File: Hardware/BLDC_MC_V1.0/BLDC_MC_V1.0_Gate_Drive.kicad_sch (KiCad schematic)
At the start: 1 part, among them U6 DRV8353HRTAR

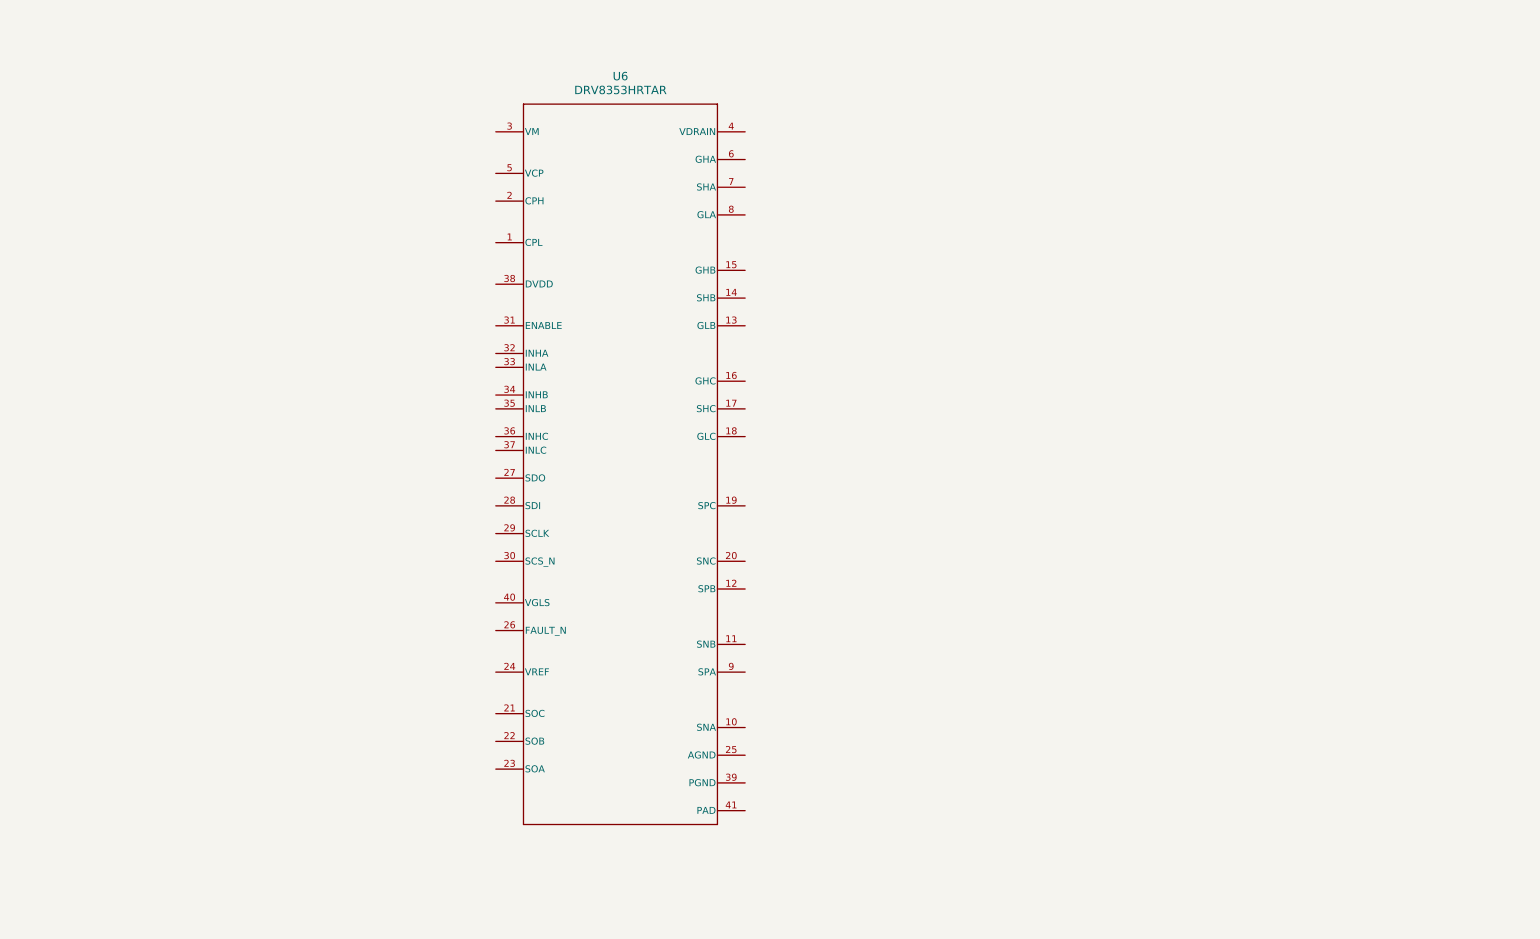
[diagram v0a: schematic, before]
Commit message: Edit the connection between sheets and add some details and connections to gatedrive sheet
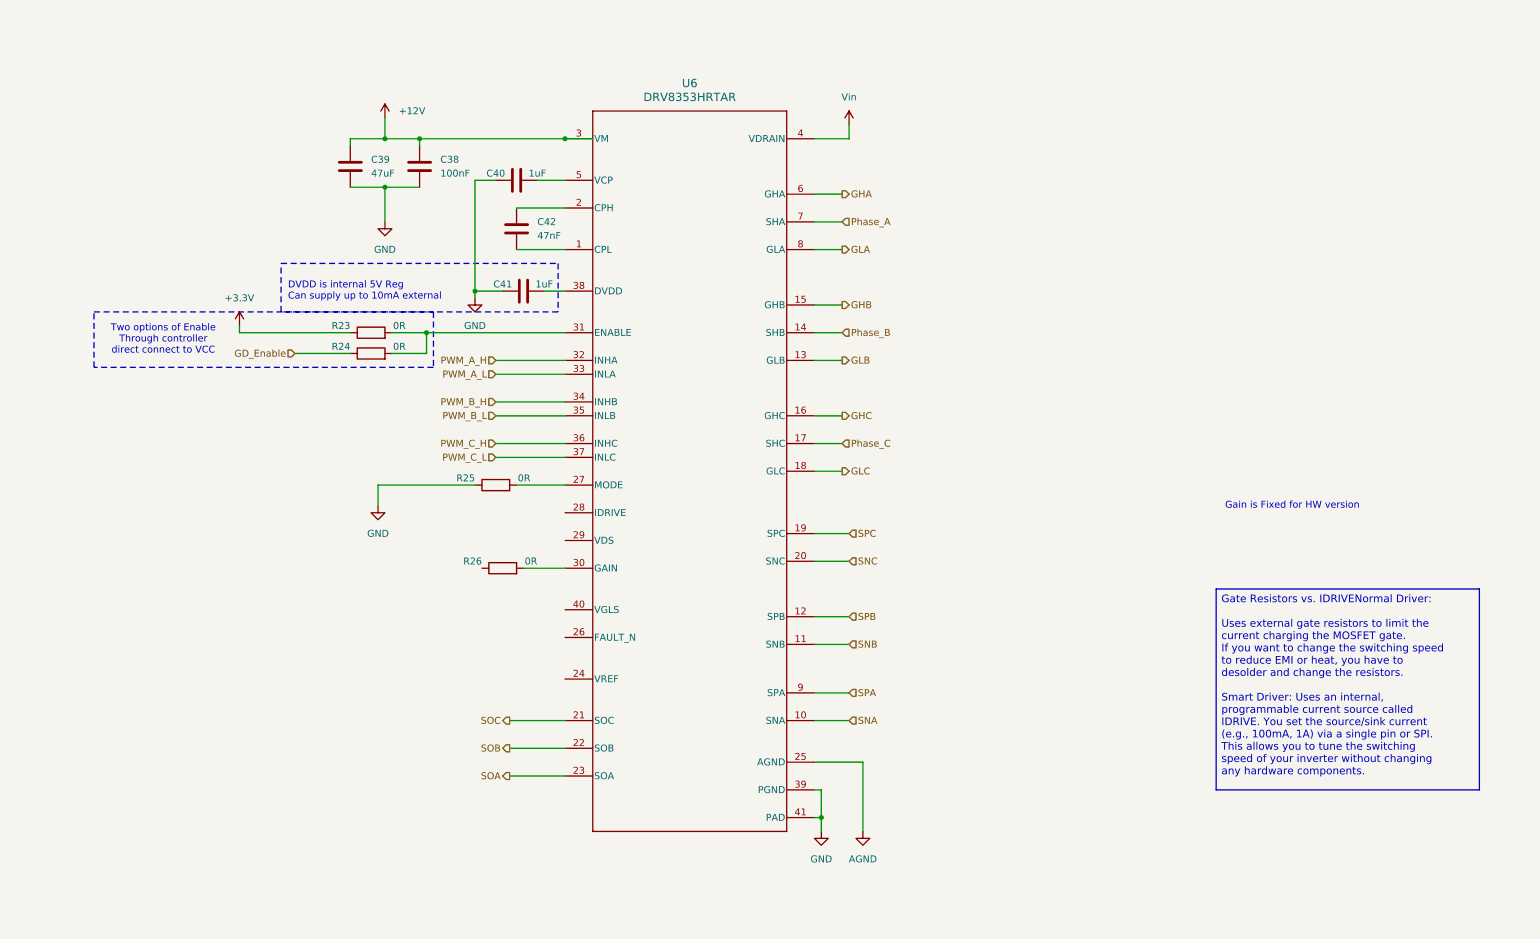
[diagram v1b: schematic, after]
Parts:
- added C38: 100nF, Capacitor_SMD:C_0805_2012Metric, symbol Device:C
- added C39: 47uF, Capacitor_SMD:C_1206_3216Metric, symbol Device:C
- added C40, C41: 1uF, Capacitor_SMD:C_0603_1608Metric, symbol Device:C
- added C42: 47nF, Capacitor_SMD:C_0603_1608Metric, symbol Device:C
- added R23, R24, R25, R26: 0R, Resistor_SMD:R_0603_1608Metric, symbol Device:R
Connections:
- net at U6.1 (CPL): now also C42.2
- net SNA: now reaches U6.10 (SNA)
- net SNB: now reaches U6.11 (SNB)
- net SPB: now reaches U6.12 (SPB)
- net GLB: now reaches U6.13 (GLB)
- net Phase_B: now reaches U6.14 (SHB)
- net GHB: now reaches U6.15 (GHB)
- net GHC: now reaches U6.16 (GHC)
- net Phase_C: now reaches U6.17 (SHC)
- net GLC: now reaches U6.18 (GLC)
- net SPC: now reaches U6.19 (SPC)
- net at U6.2 (CPH): now also C42.1
- net SNC: now reaches U6.20 (SNC)
- net SOC: now reaches U6.21 (SOC)
- net SOB: now reaches U6.22 (SOB)
- net SOA: now reaches U6.23 (SOA)
- net AGND: now reaches U6.25 (AGND)
- net at U6.27 (MODE): now also R25.2
- net +12V: now reaches U6.3 (VM)
- net +12V: now also C38.1, C39.2
- net at U6.30 (GAIN): now also R26.2
- net at U6.31 (ENABLE): now also R23.2, R24.2
- net PWM_A_H: now reaches U6.32 (INHA)
- net PWM_A_L: now reaches U6.33 (INLA)
- net PWM_B_H: now reaches U6.34 (INHB)
- net PWM_B_L: now reaches U6.35 (INLB)
- net PWM_C_H: now reaches U6.36 (INHC)
- net PWM_C_L: now reaches U6.37 (INLC)
- net at U6.38 (DVDD): now also C41.2
- net GND: now reaches U6.39 (PGND)
- net GND: now also U6.41 (PAD), C38.2, C39.1, C40.1, C41.1, R25.1
- net Vin: now reaches U6.4 (VDRAIN)
- net at U6.5 (VCP): now also C40.2
- net GHA: now reaches U6.6 (GHA)
- net Phase_A: now reaches U6.7 (SHA)
- net GLA: now reaches U6.8 (GLA)
- net SPA: now reaches U6.9 (SPA)
- new net +3.3V: R23.1
- new net GD_Enable: R24.1
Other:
- note added: "DVDD is internal 5V Reg Can supply up to 10mA external"
- note added: "Gain is Fixed for HW version"
- note added: "Two options of Enable Through controller direct connect to VCC"
- moved on the sheet: U6

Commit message: Restore the importenat project files from last commit and define the routing of current sensor as differntial pair
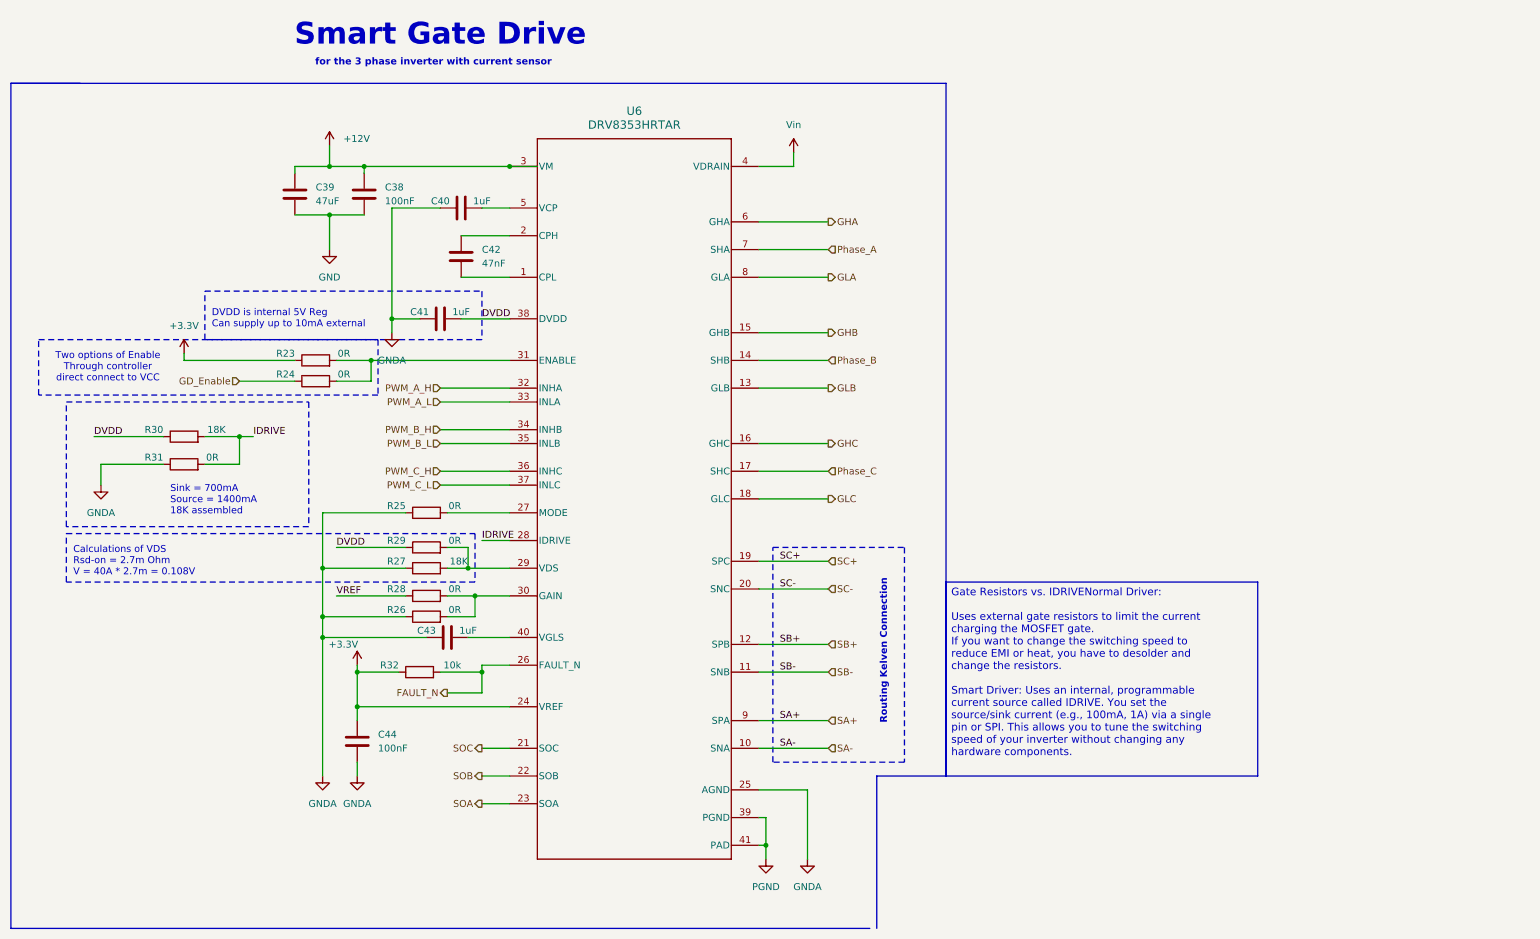
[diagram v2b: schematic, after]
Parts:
- added C43: 1uF, Capacitor_SMD:C_0603_1608Metric, symbol Device:C
- added C44: 100nF, Capacitor_SMD:C_0805_2012Metric, symbol Device:C
- added R27, R30: 18K, Resistor_SMD:R_0603_1608Metric, symbol Device:R
- added R28, R29, R31: 0R, Resistor_SMD:R_0603_1608Metric, symbol Device:R
- added R32: 10k, Resistor_SMD:R_0603_1608Metric, symbol Device:R
- R25: Assembled No -> Yes
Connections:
- net AGND is gone; now on net GNDA: U6.25 (AGND)
- net +3.3V: now also U6.24 (VREF), C44.1, R32.1
- net GND: no longer C40.1, C41.1, R25.1, U6.39 (PGND), U6.41 (PAD)
- net DVDD: now reaches C41.2, U6.38 (DVDD)
- net DVDD: now also R29.1, R30.1
- net FAULT_N: now reaches U6.26 (FAULT_N)
- net FAULT_N: now also R32.2
- net IDRIVE: now reaches U6.28 (IDRIVE)
- net IDRIVE: now also R30.2, R31.2
- net at U6.29 (VDS): now also R27.2, R29.2
- net at R26.2, U6.30 (GAIN): now also R28.2
- net at U6.40 (VGLS): now also C43.2
- net GNDA: now reaches R26.1
- net GNDA: now also C40.1, C41.1, R25.1, C43.1, C44.2, R27.1, R31.1
- net SNA renamed SA-
- net SNB renamed SB-
- net SNC renamed SC-
- net SPA renamed SA+
- net SPB renamed SB+
- net SPC renamed SC+
- new net PGND: U6.39 (PGND), U6.41 (PAD)
- new net VREF: R28.1
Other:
- note added: "Calculations of VDS Rsd-on = 2.7m Ohm V = 40A * 2.7m = 0.108V"
- note added: "Routing Kelven Connection"
- note added: "Sink = 700mA Source = 1400mA 18K assembled"
- note added: "Smart Gate Drive"
- note added: "for the 3 phase inverter with current sensor"
- note removed: "Gain is Fixed for HW version"
- moved on the sheet: C38, C39, C40, C41, C42, R23, R24, R25, R26, U6

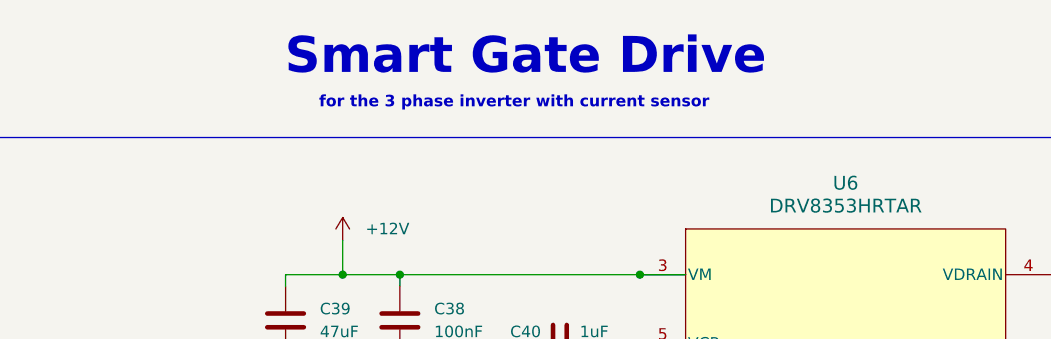
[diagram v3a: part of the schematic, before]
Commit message: Adjust the connections between sheets
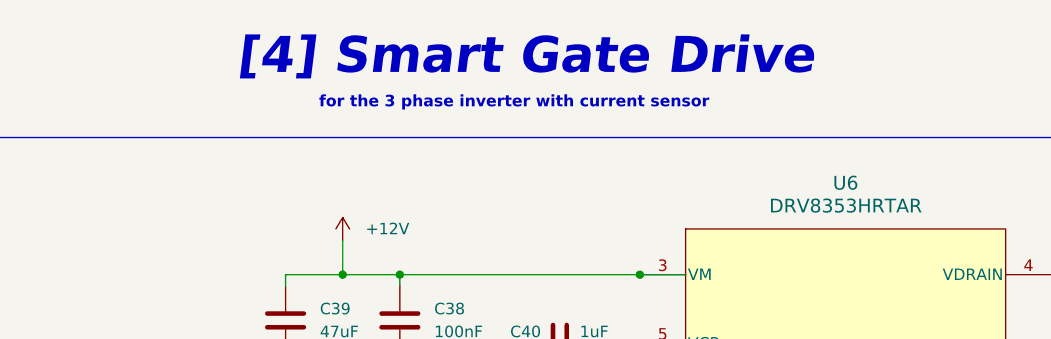
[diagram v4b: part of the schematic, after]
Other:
- note added: "[4] Smart Gate Drive"
- note removed: "Smart Gate Drive"
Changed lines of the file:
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@@
 		)
 	)
-	(text "Smart Gate Drive \n"
+	(text "[4] Smart Gate Drive \n"
 		(exclude_from_sim no)
 		(at 93.98 26.67 0)
@@
 				(thickness 0.8)
 				(bold yes)
+				(italic yes)
 				(color 132 0 0 1)
 			)

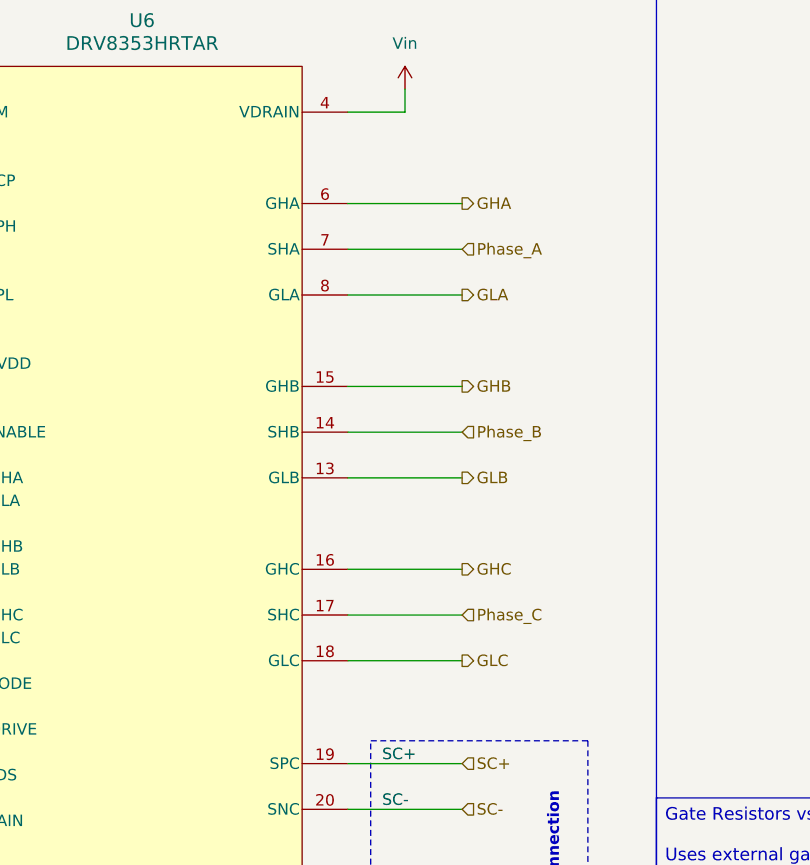
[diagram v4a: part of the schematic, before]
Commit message: Add test points for the gate drive pins
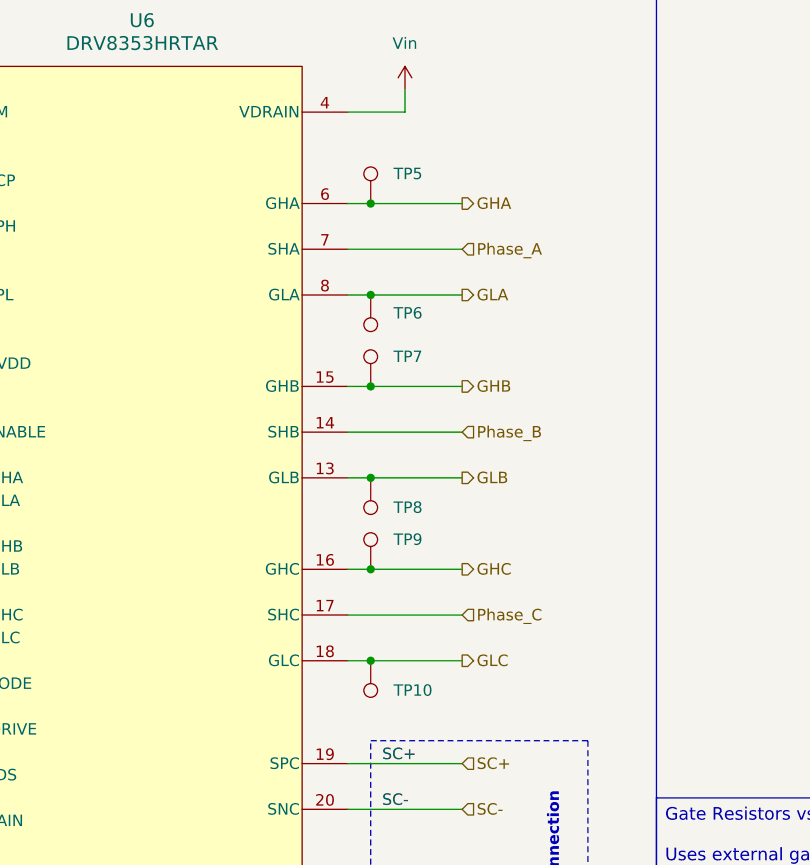
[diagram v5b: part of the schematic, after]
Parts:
- added TP10, TP5, TP6, TP7, TP8, TP9: TestPoint, Connector_Pin:Pin_D0.9mm_L10.0mm_W2.4mm_FlatFork, symbol Connector:TestPoint
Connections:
- net GHA: now also TP5.1
- net GHB: now also TP7.1
- net GHC: now also TP9.1
- net GLA: now also TP6.1
- net GLB: now also TP8.1
- net GLC: now also TP10.1

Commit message: Solve all errors and wornings in project
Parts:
- added FB2: FerriteBead, Inductor_SMD:L_0603_1608Metric, symbol Device:FerriteBead
- U6: Assembled (none) -> Yes; LCSC_PN (none) -> C2150766; MP (none) -> DRV8353HRTAR
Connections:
- net GNDA: now also FB2.2
- net PGND: now also FB2.1
- net VREF renamed Vref

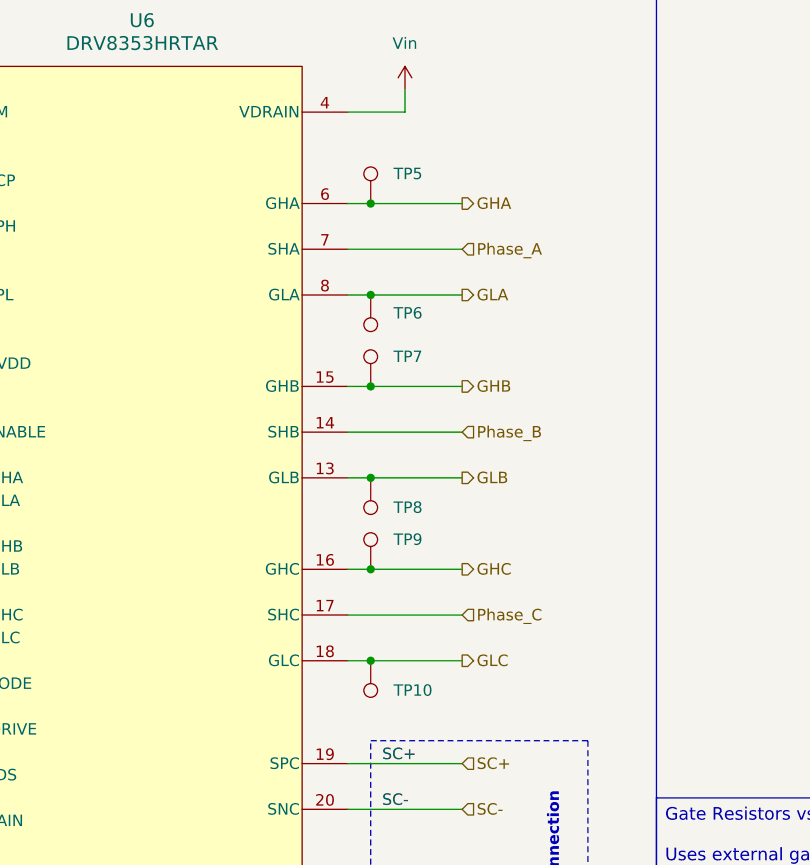
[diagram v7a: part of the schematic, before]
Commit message: Update the placement of the board
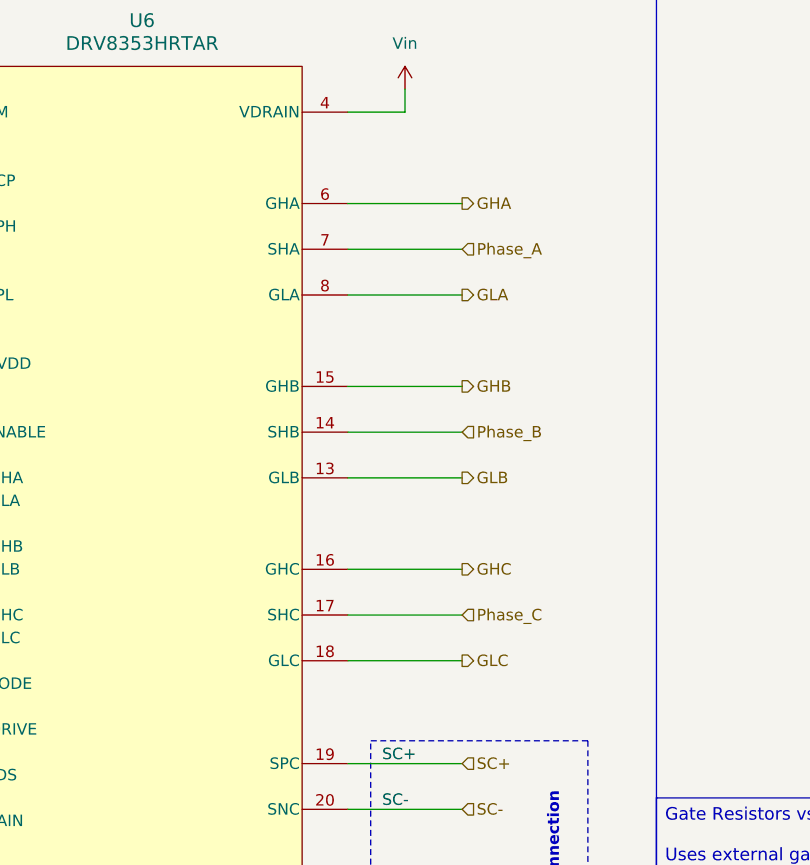
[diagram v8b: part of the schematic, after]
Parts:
- removed TP10, TP5, TP6, TP7, TP8, TP9: TestPoint, Connector_Pin:Pin_D0.9mm_L10.0mm_W2.4mm_FlatFork, symbol Connector:TestPoint
